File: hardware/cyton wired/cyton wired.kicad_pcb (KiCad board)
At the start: 4 copper layers, 61.4 x 61.3 mm, 100 parts, among them J1 Conn_02x13_Odd_Even, J2 Conn_01x08, J3 Conn_01x04, J4 Conn_01x02, J5 Conn_01x04, SW1 SW_Push, SW2 SW_Push, U1 ADS129x, U2 CP2102N-Axx-xQFN24, U3 MCP1754T-3302E/OT, U4 LM2664, U5 TPS7A24, U6 TPS723xx-Q1, U7 PIC32MX250F128B-I/SS, Y1 ABMM2-8.000MHZ-E2-T

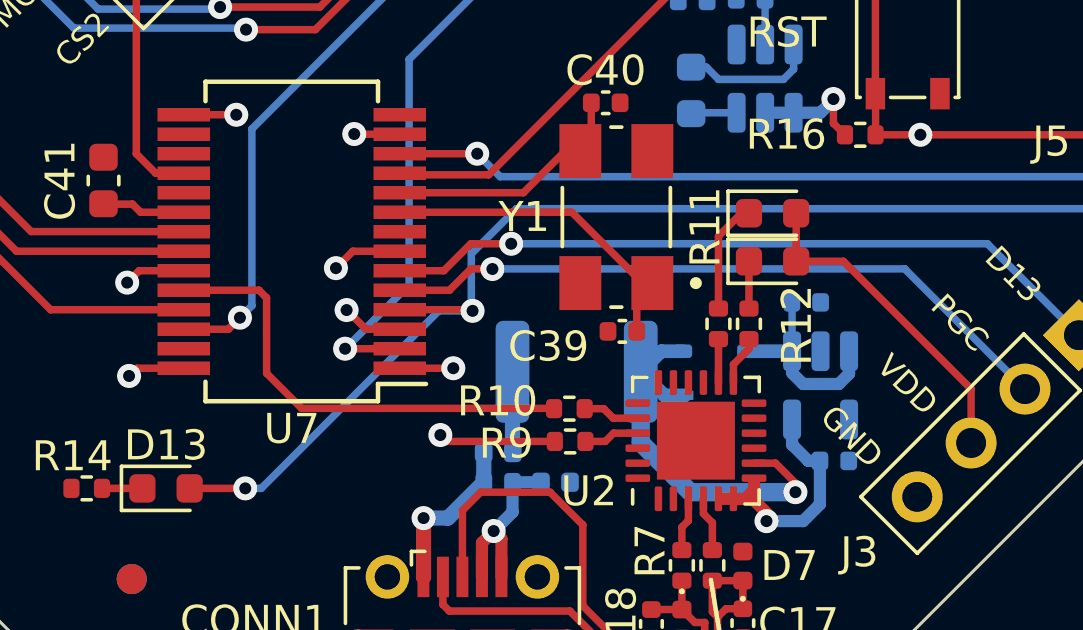
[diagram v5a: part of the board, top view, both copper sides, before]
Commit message: fixed RX and TX pins configuration
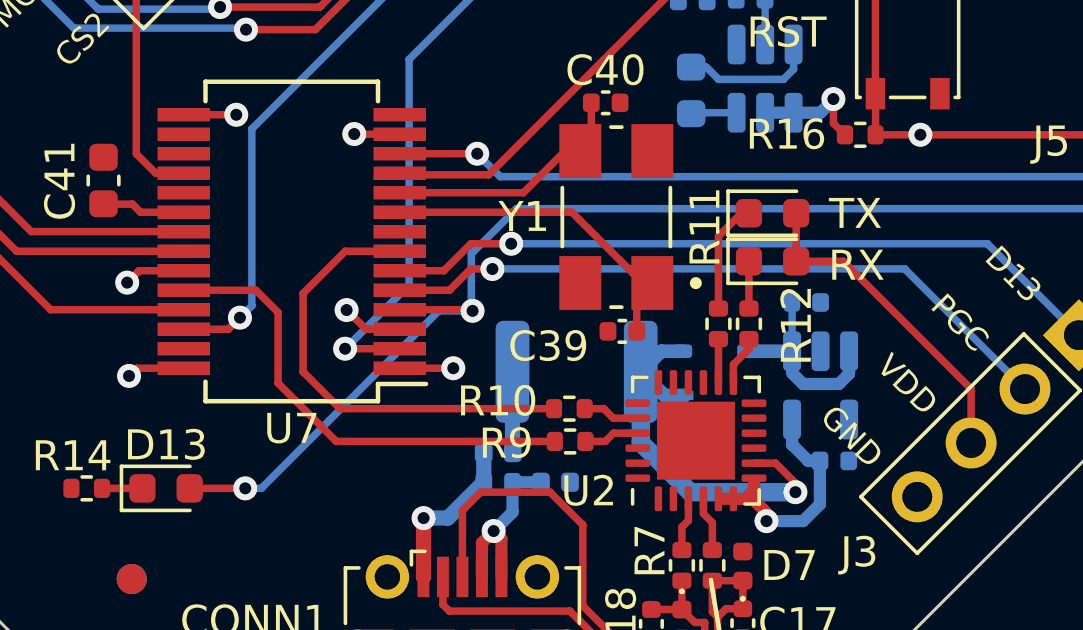
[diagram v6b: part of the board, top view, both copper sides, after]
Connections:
- R10 pad 2: /RXD -> /TO_PC
- R9 pad 2: /TXD -> /FROM_PC
- U7 pad 24: /RXD -> /FROM_PC
- U7 pad 7: /TXD -> /TO_PC
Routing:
- net /FROM_PC: track 0.00 -> 15.8 mm
- net /RXD: track 15.5 -> 0.00 mm
- net /TO_PC: track 0.00 -> 15.3 mm
- net /TXD: track 13.8 -> 0.00 mm, vias 2 -> 0
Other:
- board text added: "RX"
- board text added: "TX"
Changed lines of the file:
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@@
   (net 63 "Net-(U6-NR)")
   (net 64 "/BIAS_INV")
-  (net 65 "/RXD")
-  (net 66 "/TXD")
+  (net 65 "/FROM_PC")
+  (net 66 "/TO_PC")
   (net 67 "unconnected-(CONN1-Shield-Pad6)")
   (net 68 "Net-(D10-K)")
@@
       (net 111 "/D13") (pinfunction "D13") (pintype "input"))
     (pad "7" smd rect (at -3.6 -0.325 180) (size 1.75 0.45) (layers "F.Cu" "F.Paste" "F.Mask")
-      (net 66 "/TXD") (pinfunction "D14") (pintype "input"))
+      (net 66 "/TO_PC") (pinfunction "D14") (pintype "input"))
     (pad "8" smd rect (at -3.6 0.325 180) (size 1.75 0.45) (layers "F.Cu" "F.Paste" "F.Mask")
       (net 1 "GNDA") (pinfunction "GND") (pintype "input"))
@@
       (net 32 "VDD") (pinfunction "VDD") (pintype "input"))
     (pad "14" smd rect (at -3.6 4.225 180) (size 1.75 0.45) (layers "F.Cu" "F.Paste" "F.Mask")
-      (net 103 "/MCU/INT1") (pinfunction "D0") (pintype "input"))
+      (net 103 "/MCU/INT1") (pinfunction "D0") (pintype "input+no_connect"))
     (pad "15" smd rect (at 3.6 4.225 180) (size 1.75 0.45) (layers "F.Cu" "F.Paste" "F.Mask")
       (net 32 "VDD") (pinfunction "VBUS") (pintype "input"))
     (pad "16" smd rect (at 3.6 3.575 180) (size 1.75 0.45) (layers "F.Cu" "F.Paste" "F.Mask")
-      (net 104 "/MCU/CS4") (pinfunction "D1") (pintype "input"))
+      (net 104 "/MCU/CS4") (pinfunction "D1") (pintype "input+no_connect"))
     (pad "17" smd rect (at 3.6 2.925 180) (size 1.75 0.45) (layers "F.Cu" "F.Paste" "F.Mask")
-      (net 105 "/MCU/CS3") (pinfunction "D2") (pintype "input"))
+      (net 105 "/MCU/CS3") (pinfunction "D2") (pintype "input+no_connect"))
     (pad "18" smd rect (at 3.6 2.275 180) (size 1.75 0.45) (layers "F.Cu" "F.Paste" "F.Mask")
       (net 62 "/CS2") (pinfunction "D3") (pintype "input"))
@@
       (net 32 "VDD") (pinfunction "VDD") (pintype "input"))
     (pad "24" smd rect (at 3.6 -1.625 180) (size 1.75 0.45) (layers "F.Cu" "F.Paste" "F.Mask")
-      (net 65 "/RXD") (pinfunction "D6") (pintype "input"))
+      (net 65 "/FROM_PC") (pinfunction "D6") (pintype "input"))
     (pad "25" smd rect (at 3.6 -2.275 180) (size 1.75 0.45) (layers "F.Cu" "F.Paste" "F.Mask")
       (net 58 "/SCLK") (pinfunction "D7") (pintype "input"))
@@
       (net 74 "Net-(U2-RXD)") (pintype "passive"))
     (pad "2" smd roundrect (at 0.51 0 180) (size 0.54 0.64) (layers "F.Cu" "F.Paste" "F.Mask") (roundrect_rratio 0.25)
-      (net 65 "/RXD") (pintype "passive"))
+      (net 66 "/TO_PC") (pintype "passive"))
     (model "${KICAD6_3DMODEL_DIR}/Resistor_SMD.3dshapes/R_0402_1005Metric.wrl"
       (offset (xyz 0 0 0))
@@
       (net 73 "Net-(U2-TXD)") (pintype "passive"))
     (pad "2" smd roundrect (at 0.51 0 180) (size 0.54 0.64) (layers "F.Cu" "F.Paste" "F.Mask") (roundrect_rratio 0.25)
-      (net 66 "/TXD") (pintype "passive"))
+      (net 65 "/FROM_PC") (pintype "passive"))
     (model "${KICAD6_3DMODEL_DIR}/Resistor_SMD.3dshapes/R_0402_1005Metric.wrl"
       (offset (xyz 0 0 0))
@@
     (effects (font (size 0.762 0.762) (thickness 0.15)) (justify left bottom))
   )
+  (gr_text "TX" (at 151.9174 121.8692) (layer "F.SilkS")
+    (effects (font (size 1 1) (thickness 0.15)) (justify left bottom))
+  )
   (gr_text "CLK" (at 123.1392 112.9284 45) (layer "F.SilkS")
     (effects (font (size 0.762 0.762) (thickness 0.15)) (justify left bottom))
@@
     (effects (font (size 0.762 0.762) (thickness 0.15)) (justify left bottom))
   )
+  (gr_text "RX" (at 151.892 123.5964) (layer "F.SilkS")
+    (effects (font (size 1 1) (thickness 0.15)) (justify left bottom))
+  )
   (gr_text "PGD" (at 164.6682 123.1138) (layer "F.SilkS")
     (effects (font (size 0.762 0.762) (thickness 0.15)) (justify left bottom))
@@
   (segment (start 144.2974 99.6188) (end 148.8948 99.6188) (width 0.2032) (layer "F.Cu") (net 64))
   (segment (start 148.8948 99.6188) (end 149.9108 98.6028) (width 0.2032) (layer "F.Cu") (net 64))
-  (segment (start 133.1722 124.079) (end 133.1722 126.5936) (width 0.25) (layer "F.Cu") (net 65))
-  (segment (start 133.1722 126.5936) (end 134.3406 127.762) (width 0.25) (layer "F.Cu") (net 65))
-  (segment (start 142.744 127.762) (end 142.7544 127.7724) (width 0.25) (layer "F.Cu") (net 65))
-  (segment (start 132.9176 123.8244) (end 133.1722 124.079) (width 0.25) (layer "F.Cu") (net 65))
-  (segment (start 134.3406 127.762) (end 142.744 127.762) (width 0.25) (layer "F.Cu") (net 65))
-  (segment (start 130.4104 123.8244) (end 132.9176 123.8244) (width 0.25) (layer "F.Cu") (net 65))
-  (segment (start 139.177 128.8646) (end 138.9634 128.651) (width 0.25) (layer "F.Cu") (net 66))
-  (segment (start 136.0476 122.5244) (end 137.6104 122.5244) (width 0.25) (layer "F.Cu") (net 66))
-  (segment (start 142.7798 128.8646) (end 139.177 128.8646) (width 0.25) (layer "F.Cu") (net 66))
-  (segment (start 135.4836 123.0884) (end 136.0476 122.5244) (width 0.25) (layer "F.Cu") (net 66))
-  (via (at 138.9634 128.651) (size 0.8) (drill 0.4) (layers "F.Cu" "B.Cu") (net 66))
-  (via (at 135.4836 123.0884) (size 0.8) (drill 0.4) (layers "F.Cu" "B.Cu") (net 66))
-  (segment (start 136.4488 123.0884) (end 135.4836 123.0884) (width 0.25) (layer "In2.Cu") (net 66))
-  (segment (start 137.5664 127.254) (end 137.5664 124.206) (width 0.25) (layer "In2.Cu") (net 66))
-  (segment (start 138.9634 128.651) (end 137.5664 127.254) (width 0.25) (layer "In2.Cu") (net 66))
-  (segment (start 137.5664 124.206) (end 136.4488 123.0884) (width 0.25) (layer "In2.Cu") (net 66))
+  (segment (start 133.5532 126.9238) (end 135.494 128.8646) (width 0.25) (layer "F.Cu") (net 65))
+  (segment (start 130.4104 123.8244) (end 132.816 123.8244) (width 0.25) (layer "F.Cu") (net 65))
+  (segment (start 133.5532 124.5616) (end 133.5532 126.9238) (width 0.25) (layer "F.Cu") (net 65))
+  (segment (start 132.816 123.8244) (end 133.5532 124.5616) (width 0.25) (layer "F.Cu") (net 65))
+  (segment (start 135.494 128.8646) (end 142.7798 128.8646) (width 0.25) (layer "F.Cu") (net 65))
+  (segment (start 134.3891 126.5451) (end 134.3891 123.9289) (width 0.25) (layer "F.Cu") (net 66))
+  (segment (start 142.7544 127.7724) (end 135.6164 127.7724) (width 0.25) (layer "F.Cu") (net 66))
+  (segment (start 135.6164 127.7724) (end 134.3891 126.5451) (width 0.25) (layer "F.Cu") (net 66))
+  (segment (start 135.7936 122.5244) (end 137.6104 122.5244) (width 0.25) (layer "F.Cu") (net 66))
+  (segment (start 134.3891 123.9289) (end 135.7936 122.5244) (width 0.25) (layer "F.Cu") (net 66))
+  (segment (start 142.744 127.762) (end 142.7544 127.7724) (width 0.25) (layer "F.Cu") (net 66))
   (segment (start 148.2344 122.0216) (end 148.2344 124.4346) (width 0.25) (layer "F.Cu") (net 68))
   (segment (start 148.9964 121.2596) (end 148.2344 122.0216) (width 0.25) (layer "F.Cu") (net 68))

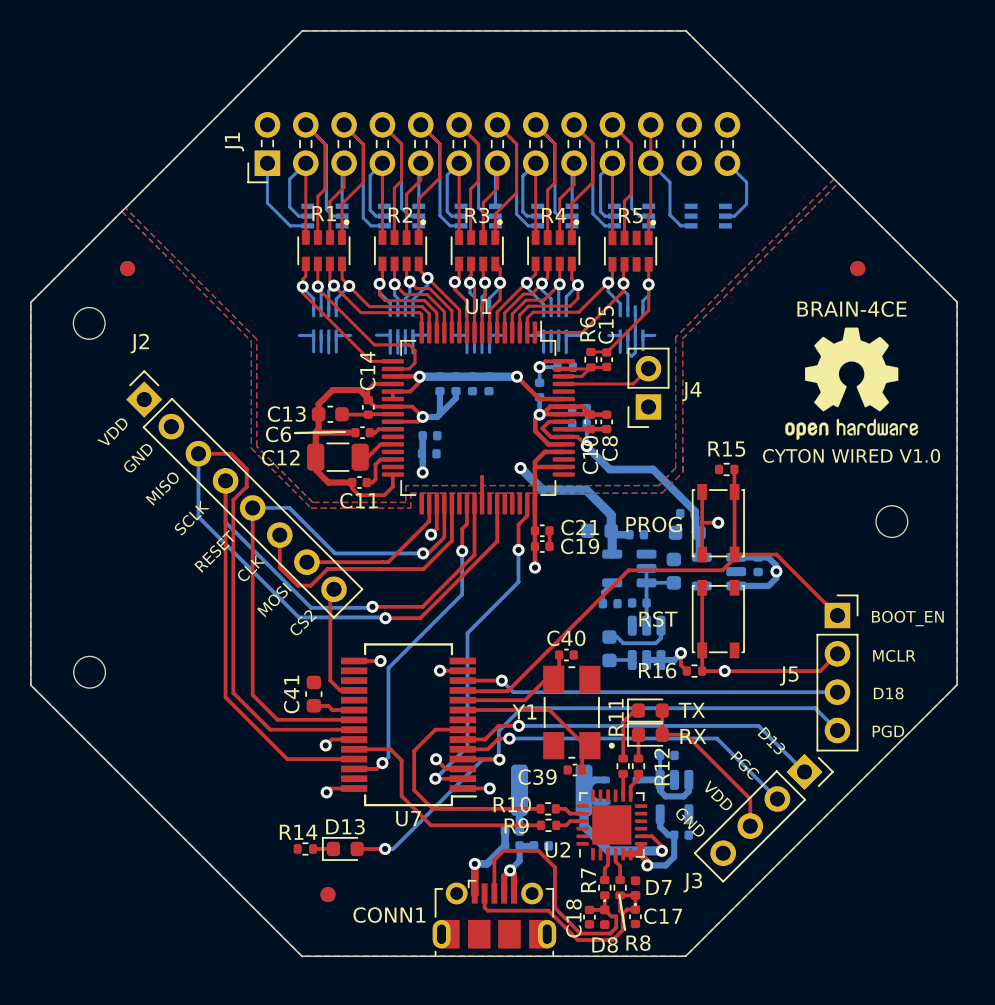
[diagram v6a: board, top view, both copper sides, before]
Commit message: enlarged mounting holes
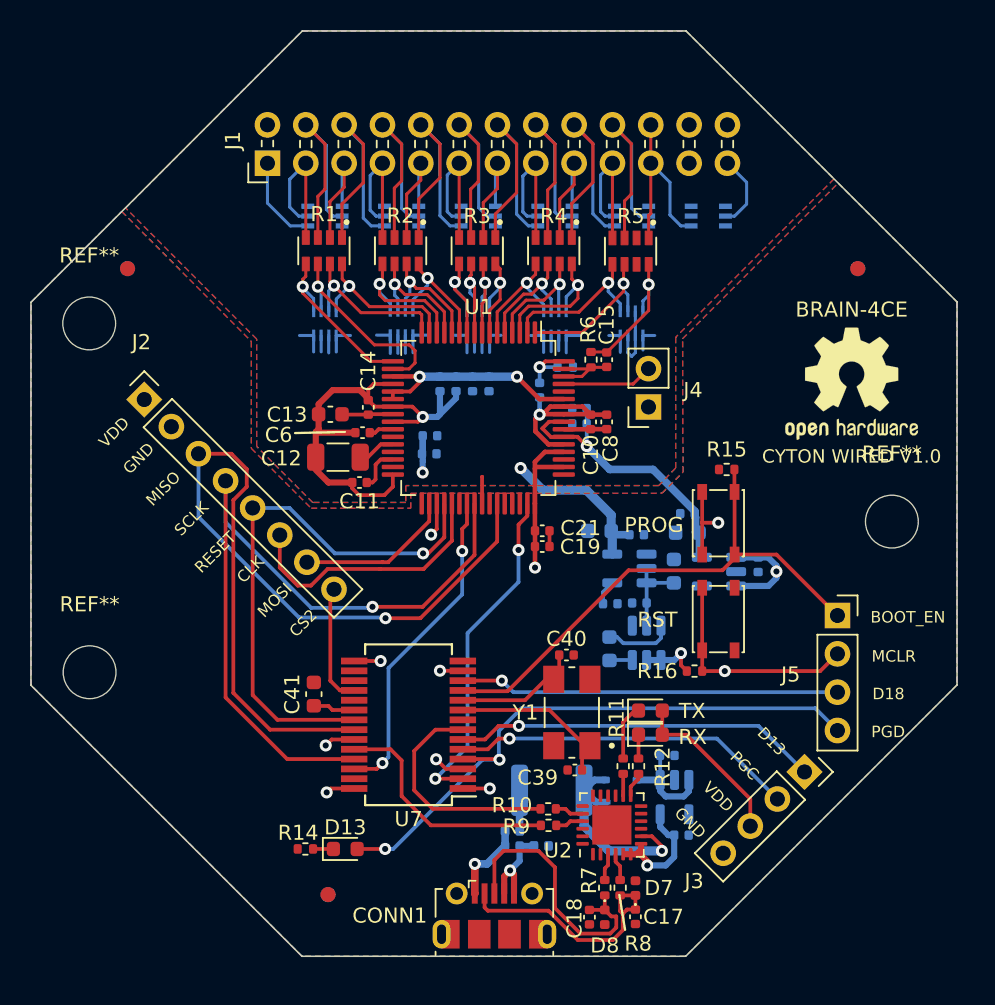
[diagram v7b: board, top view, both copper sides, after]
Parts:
- removed ? (x2): , 
- removed the REF** at (166.0, 108.7)
- added REF**: MountingHole_3.5mm, MountingHole:MountingHole_3.5mm, F.Cu at (112.9, 95.6)
- added REF**: MountingHole_3.5mm, MountingHole:MountingHole_3.5mm, F.Cu at (166.0, 108.7)
- added REF**: MountingHole_3.5mm, MountingHole:MountingHole_3.5mm, F.Cu at (112.9, 118.7)
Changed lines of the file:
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@@
       (solder_mask_margin 0.5) (clearance 0.5))
   )
-  (footprint "" (layer "F.Cu")
-    (at 112.8776 118.7196)
-    (fp_text reference "" (at 0 0) (layer "F.SilkS")
-        (effects (font (size 1.27 1.27) (thickness 0.15)))
+  (footprint "MountingHole:MountingHole_3.5mm" (layer "F.Cu")
+    (at 112.8522 95.6056)
+    (descr "Mounting Hole 3.5mm, no annular")
+    (tags "mounting hole 3.5mm no annular")
+    (attr exclude_from_pos_files exclude_from_bom)
+    (fp_text reference "REF**" (at 0 -4.5) (layer "F.SilkS")
+        (effects (font (size 1 1) (thickness 0.15)))
     )
-    (fp_text value "" (at 0 0) (layer "F.SilkS")
-        (effects (font (size 1.27 1.27) (thickness 0.15)))
+    (fp_text value "MountingHole_3.5mm" (at 0 4.5) (layer "F.Fab")
+        (effects (font (size 1 1) (thickness 0.15)))
     )
-    (pad "" np_thru_hole circle (at 0 0) (size 2.1 2.1) (drill 2.1) (layers "*.Cu" "*.Mask"))
+    (fp_text user "${REFERENCE}" (at 0 0) (layer "F.Fab")
+        (effects (font (size 1 1) (thickness 0.15)))
+    )
+    (fp_circle (center 0 0) (end 3.5 0)
+      (stroke (width 0.15) (type solid)) (fill none) (layer "Cmts.User"))
+    (fp_circle (center 0 0) (end 3.75 0)
+      (stroke (width 0.05) (type solid)) (fill none) (layer "F.CrtYd"))
+    (pad "" np_thru_hole circle (at 0 0) (size 3.5 3.5) (drill 3.5) (layers "*.Cu" "*.Mask"))
   )
   (footprint "Resistor_SMD:R_0402_1005Metric" (layer "F.Cu")
@@
     )
   )
-  (footprint "MountingHole:MountingHole_2.1mm" (layer "F.Cu")
-    (at 166.0398 108.7374)
-    (descr "Mounting Hole 2.1mm, no annular")
-    (tags "mounting hole 2.1mm no annular")
-    (attr exclude_from_pos_files exclude_from_bom)
-    (fp_text reference "REF**" (at 0 -3.2) (layer "F.SilkS") hide
-        (effects (font (size 1 1) (thickness 0.15)))
-    )
-    (fp_text value "MountingHole_2.1mm" (at 0 3.2) (layer "F.Fab")
-        (effects (font (size 1 1) (thickness 0.15)))
-    )
-    (fp_text user "${REFERENCE}" (at 0 0) (layer "F.Fab")
-        (effects (font (size 1 1) (thickness 0.15)))
-    )
-    (fp_circle (center 0 0) (end 2.1 0)
-      (stroke (width 0.15) (type solid)) (fill none) (layer "Cmts.User"))
-    (fp_circle (center 0 0) (end 2.35 0)
-      (stroke (width 0.05) (type solid)) (fill none) (layer "F.CrtYd"))
-    (pad "" np_thru_hole circle (at 0 0) (size 2.1 2.1) (drill 2.1) (layers "*.Cu" "*.Mask"))
-  )
   (footprint "Capacitor_SMD:C_0402_1005Metric" (layer "F.Cu")
     (at 149.0472 134.9222 -90)
@@
     )
   )
+  (footprint "MountingHole:MountingHole_3.5mm" (layer "F.Cu")
+    (at 166.0398 108.7374)
+    (descr "Mounting Hole 3.5mm, no annular")
+    (tags "mounting hole 3.5mm no annular")
+    (attr exclude_from_pos_files exclude_from_bom)
+    (fp_text reference "REF**" (at 0 -4.5) (layer "F.SilkS")
+        (effects (font (size 1 1) (thickness 0.15)))
+    )
+    (fp_text value "MountingHole_3.5mm" (at 0 4.5) (layer "F.Fab")
+        (effects (font (size 1 1) (thickness 0.15)))
+    )
+    (fp_text user "${REFERENCE}" (at 0 0) (layer "F.Fab")
+        (effects (font (size 1 1) (thickness 0.15)))
+    )
+    (fp_circle (center 0 0) (end 3.5 0)
+      (stroke (width 0.15) (type solid)) (fill none) (layer "Cmts.User"))
+    (fp_circle (center 0 0) (end 3.75 0)
+      (stroke (width 0.05) (type solid)) (fill none) (layer "F.CrtYd"))
+    (pad "" np_thru_hole circle locked (at 0 0) (size 3.5 3.5) (drill 3.5) (layers "*.Cu" "*.Mask"))
+  )
   (footprint "Diode_SMD:D_0402_1005Metric" (layer "F.Cu")
     (at 147.0152 134.9526 -90)
@@
     )
   )
+  (footprint "MountingHole:MountingHole_3.5mm" (layer "F.Cu")
+    (at 112.8776 118.7196)
+    (descr "Mounting Hole 3.5mm, no annular")
+    (tags "mounting hole 3.5mm no annular")
+    (attr exclude_from_pos_files exclude_from_bom)
+    (fp_text reference "REF**" (at 0 -4.5) (layer "F.SilkS")
+        (effects (font (size 1 1) (thickness 0.15)))
+    )
+    (fp_text value "MountingHole_3.5mm" (at 0 4.5) (layer "F.Fab")
+        (effects (font (size 1 1) (thickness 0.15)))
+    )
+    (fp_text user "${REFERENCE}" (at 0 0) (layer "F.Fab")
+        (effects (font (size 1 1) (thickness 0.15)))
+    )
+    (fp_circle (center 0 0) (end 3.5 0)
+      (stroke (width 0.15) (type solid)) (fill none) (layer "Cmts.User"))
+    (fp_circle (center 0 0) (end 3.75 0)
+      (stroke (width 0.05) (type solid)) (fill none) (layer "F.CrtYd"))
+    (pad "" np_thru_hole circle (at 0 0) (size 3.5 3.5) (drill 3.5) (layers "*.Cu" "*.Mask"))
+  )
   (footprint "Resistor Arrays:RESCAF80P320X160X60-8N" (layer "F.Cu")
     (at 143.6306 90.791 -90)
@@
     )
   )
-  (footprint "" (layer "F.Cu")
-    (at 112.8522 95.6056)
-    (fp_text reference "" (at 0 0) (layer "F.SilkS")
-        (effects (font (size 1.27 1.27) (thickness 0.15)))
-    )
-    (fp_text value "" (at 0 0) (layer "F.SilkS")
-        (effects (font (size 1.27 1.27) (thickness 0.15)))
-    )
-    (pad "" np_thru_hole circle (at 0 0) (size 2.1 2.1) (drill 2.1) (layers "*.Cu" "*.Mask"))
-  )
   (footprint "Button_Switch_SMD:SW_SPST_PTS810" (layer "F.Cu")
